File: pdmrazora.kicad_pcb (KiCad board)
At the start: 2 copper layers, 15 parts, among them J1 9-6437287-8, J2 M6_VBAT_GND, M1000 Module:mega-mcu144/0.7, U1 BTS50010-1TAD, U11 BTS7004-1EPP, U12 BTS7004-1EPP, U13 BTS7004-1EPP, U14 BTS7004-1EPP, U15 BTS7004-1EPP, U16 BTS7004-1EPP, U17 BTS7004-1EPP, U18 BTS7004-1EPP, U2 BTS50010-1TAD, U3 BTS50010-1TAD, U4 BTS50010-1TAD

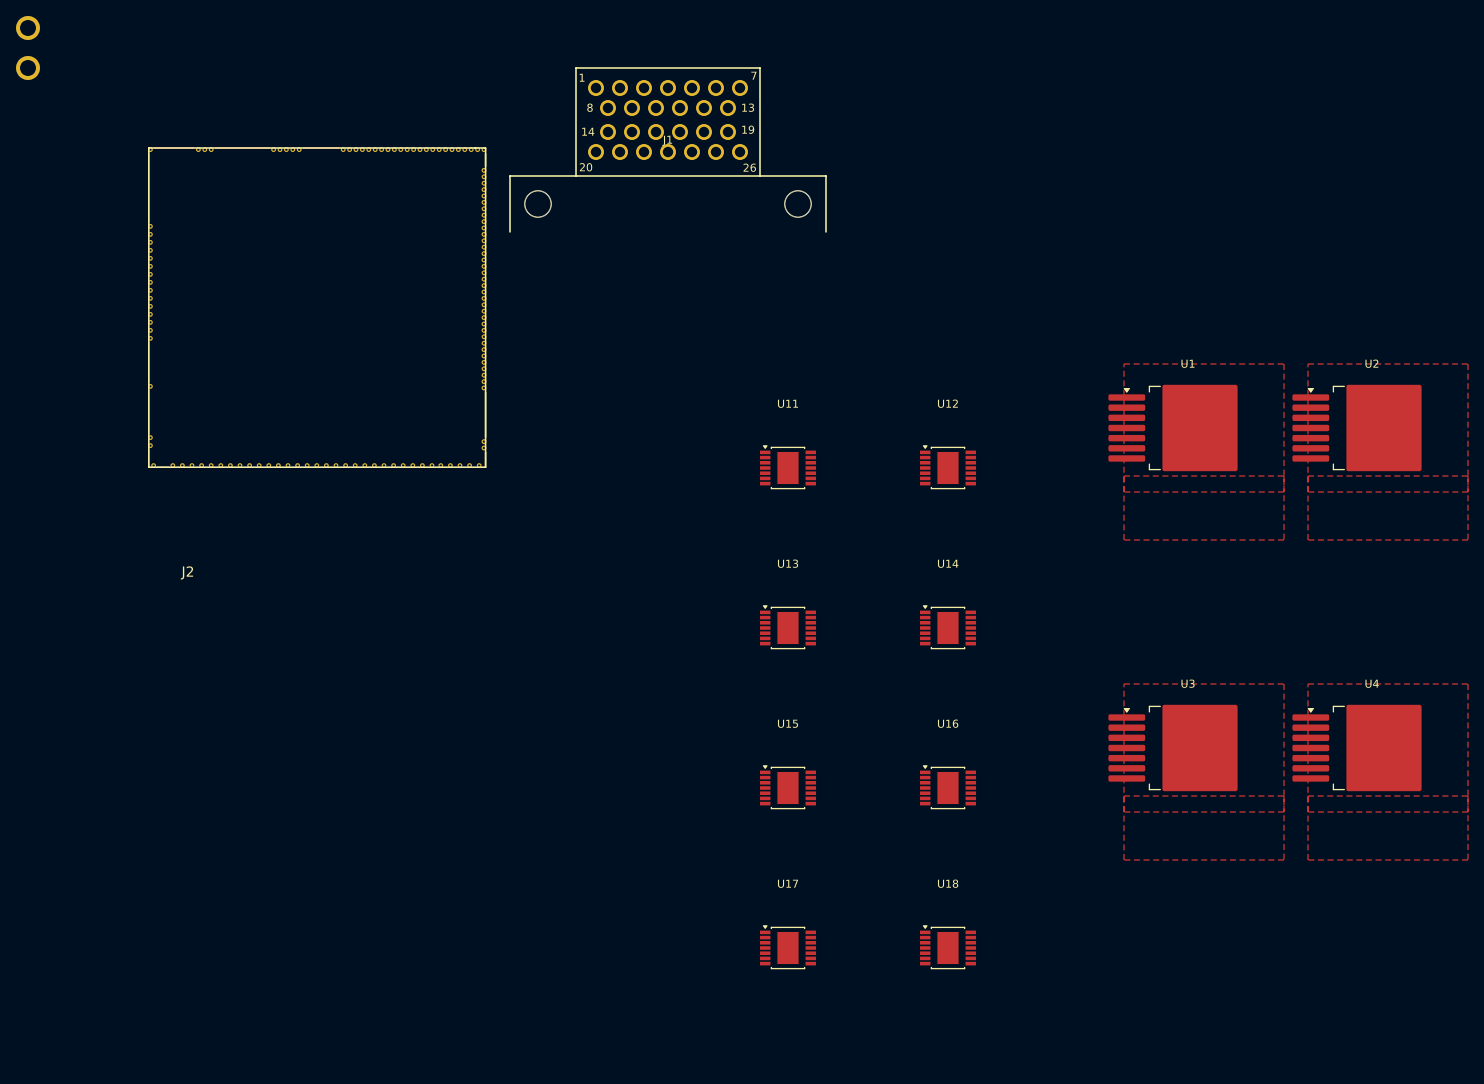
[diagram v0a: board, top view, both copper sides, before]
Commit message: Nest PDM floorplan and add power/ADIO pour scaffolding
Rearrange all 53 footprints onto a 150×130 mm Edge.Cuts board (aux
origin bottom-left), with M1000 clear for Hellen merge, J1 on the
bottom edge, HP/ADIO clustered with local sense passives, and pour
outlines for VBAT/GND/PWR_OUT/ADIO. Length routing of control/sense
remains ratsnest after fill — aggressive autoroute introduced shorts.
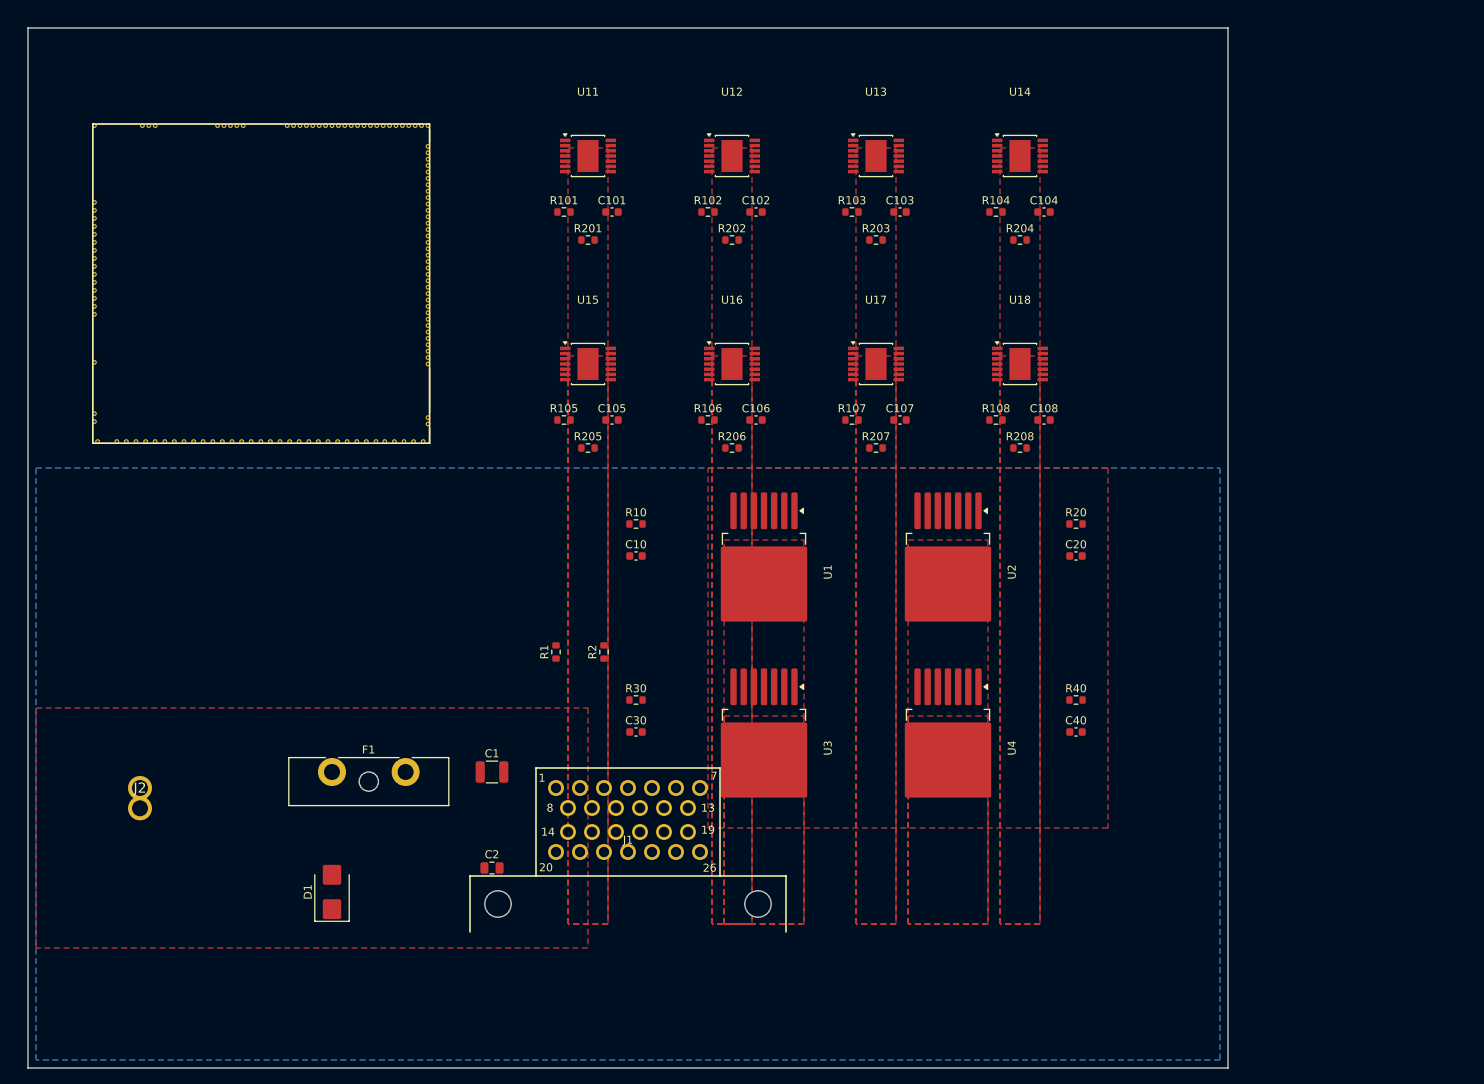
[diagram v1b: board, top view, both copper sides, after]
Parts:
- added C1: 100u_50V, C_1210_3225Metric, F.Cu at (58.0, 93.0)
- added C10: 10n, C_0603_1608Metric, F.Cu at (76.0, 66.0)
- added C101: 10n, C_0603_1608Metric, F.Cu at (73.0, 23.0)
- added C102: 10n, C_0603_1608Metric, F.Cu at (91.0, 23.0)
- added C103: 10n, C_0603_1608Metric, F.Cu at (109.0, 23.0)
- added C104: 10n, C_0603_1608Metric, F.Cu at (127.0, 23.0)
- added C105: 10n, C_0603_1608Metric, F.Cu at (73.0, 49.0)
- added C106: 10n, C_0603_1608Metric, F.Cu at (91.0, 49.0)
- added C107: 10n, C_0603_1608Metric, F.Cu at (109.0, 49.0)
- added C108: 10n, C_0603_1608Metric, F.Cu at (127.0, 49.0)
- added C2: 100n, C_0805_2012Metric, F.Cu at (58.0, 105.0)
- added C20: 10n, C_0603_1608Metric, F.Cu at (131.0, 66.0)
- added C30: 10n, C_0603_1608Metric, F.Cu at (76.0, 88.0)
- added C40: 10n, C_0603_1608Metric, F.Cu at (131.0, 88.0)
- added D1: SMBJ33CA, D_SMB, F.Cu at (38.0, 108.0)
- added F1: 150A_MEGA_TBD, Fuseholder_Blade_ATO_Littelfuse_Pudenz_2_Pin, F.Cu at (38.0, 93.0)
- added R1: 100k, R_0603_1608Metric, F.Cu at (66.0, 78.0)
- added R10: 2k7, R_0603_1608Metric, F.Cu at (76.0, 62.0)
- added R101: 4k7, R_0603_1608Metric, F.Cu at (67.0, 23.0)
- added R102: 4k7, R_0603_1608Metric, F.Cu at (85.0, 23.0)
- added R103: 4k7, R_0603_1608Metric, F.Cu at (103.0, 23.0)
- added R104: 4k7, R_0603_1608Metric, F.Cu at (121.0, 23.0)
- added R105: 4k7, R_0603_1608Metric, F.Cu at (67.0, 49.0)
- added R106: 4k7, R_0603_1608Metric, F.Cu at (85.0, 49.0)
- added R107: 4k7, R_0603_1608Metric, F.Cu at (103.0, 49.0)
- added R108: 4k7, R_0603_1608Metric, F.Cu at (121.0, 49.0)
- added R2: 10k, R_0603_1608Metric, F.Cu at (72.0, 78.0)
- added R20: 2k7, R_0603_1608Metric, F.Cu at (131.0, 62.0)
- added R201: 4k7, R_0603_1608Metric, F.Cu at (70.0, 26.5)
- added R202: 4k7, R_0603_1608Metric, F.Cu at (88.0, 26.5)
- added R203: 4k7, R_0603_1608Metric, F.Cu at (106.0, 26.5)
- added R204: 4k7, R_0603_1608Metric, F.Cu at (124.0, 26.5)
- added R205: 4k7, R_0603_1608Metric, F.Cu at (70.0, 52.5)
- added R206: 4k7, R_0603_1608Metric, F.Cu at (88.0, 52.5)
- added R207: 4k7, R_0603_1608Metric, F.Cu at (106.0, 52.5)
- added R208: 4k7, R_0603_1608Metric, F.Cu at (124.0, 52.5)
- added R30: 2k7, R_0603_1608Metric, F.Cu at (76.0, 84.0)
- added R40: 2k7, R_0603_1608Metric, F.Cu at (131.0, 84.0)
- moved J1 87.6 mm to (75.0, 109.5)
- moved U17 73.8 mm to (106.0, 42.0)
- moved U18 73.6 mm to (124.0, 42.0)
- moved U13 60.0 mm to (106.0, 16.0)
- moved U14 59.7 mm to (124.0, 16.0)
- moved U16 59.5 mm to (88.0, 42.0)
- moved U15 58.6 mm to (70.0, 42.0)
- moved U1 56.0 mm to (92.0, 68.0), turned to -90 degrees
- moved U2 56.0 mm to (115.0, 68.0), turned to -90 degrees
- moved U3 53.0 mm to (92.0, 90.0), turned to -90 degrees
- moved U4 53.0 mm to (115.0, 90.0), turned to -90 degrees
- moved U12 47.4 mm to (88.0, 16.0)
- moved U11 46.3 mm to (70.0, 16.0)
- moved J2 27.7 mm to (14.0, 95.0)
- moved M1000 7.62 mm to (8.00, 52.0)
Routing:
- added copper zone on F.Cu, net ADIO1
- added copper zone on F.Cu, net ADIO2
- added copper zone on F.Cu, net ADIO3
- added copper zone on F.Cu, net ADIO4
- added copper zone on F.Cu, net ADIO5
- added copper zone on F.Cu, net ADIO6
- added copper zone on F.Cu, net ADIO7
- added copper zone on F.Cu, net ADIO8
- added copper zone on B.Cu, net GND
- added copper zone on F.Cu, net GND
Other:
- board outline added: 150 x 130 mm

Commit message: Fill pours and selectively route copper on pdmrazora
Complete zone fills for VBAT/GND/PWR_OUT/ADIO (M1000 keepout
respected) and add selective Manhattan tracks + vias for power
entry, HP/ADIO outs, local sense, IGN/CAN/SENSOR spines, and
EN/IS stubs to M1000. Tracks 0→328, DRC unconnected 254→97.
KiCad 8 headers preserved after pcbnew 9 save. Interactive DRC
cleanup of remaining shorts/crossings still needed.
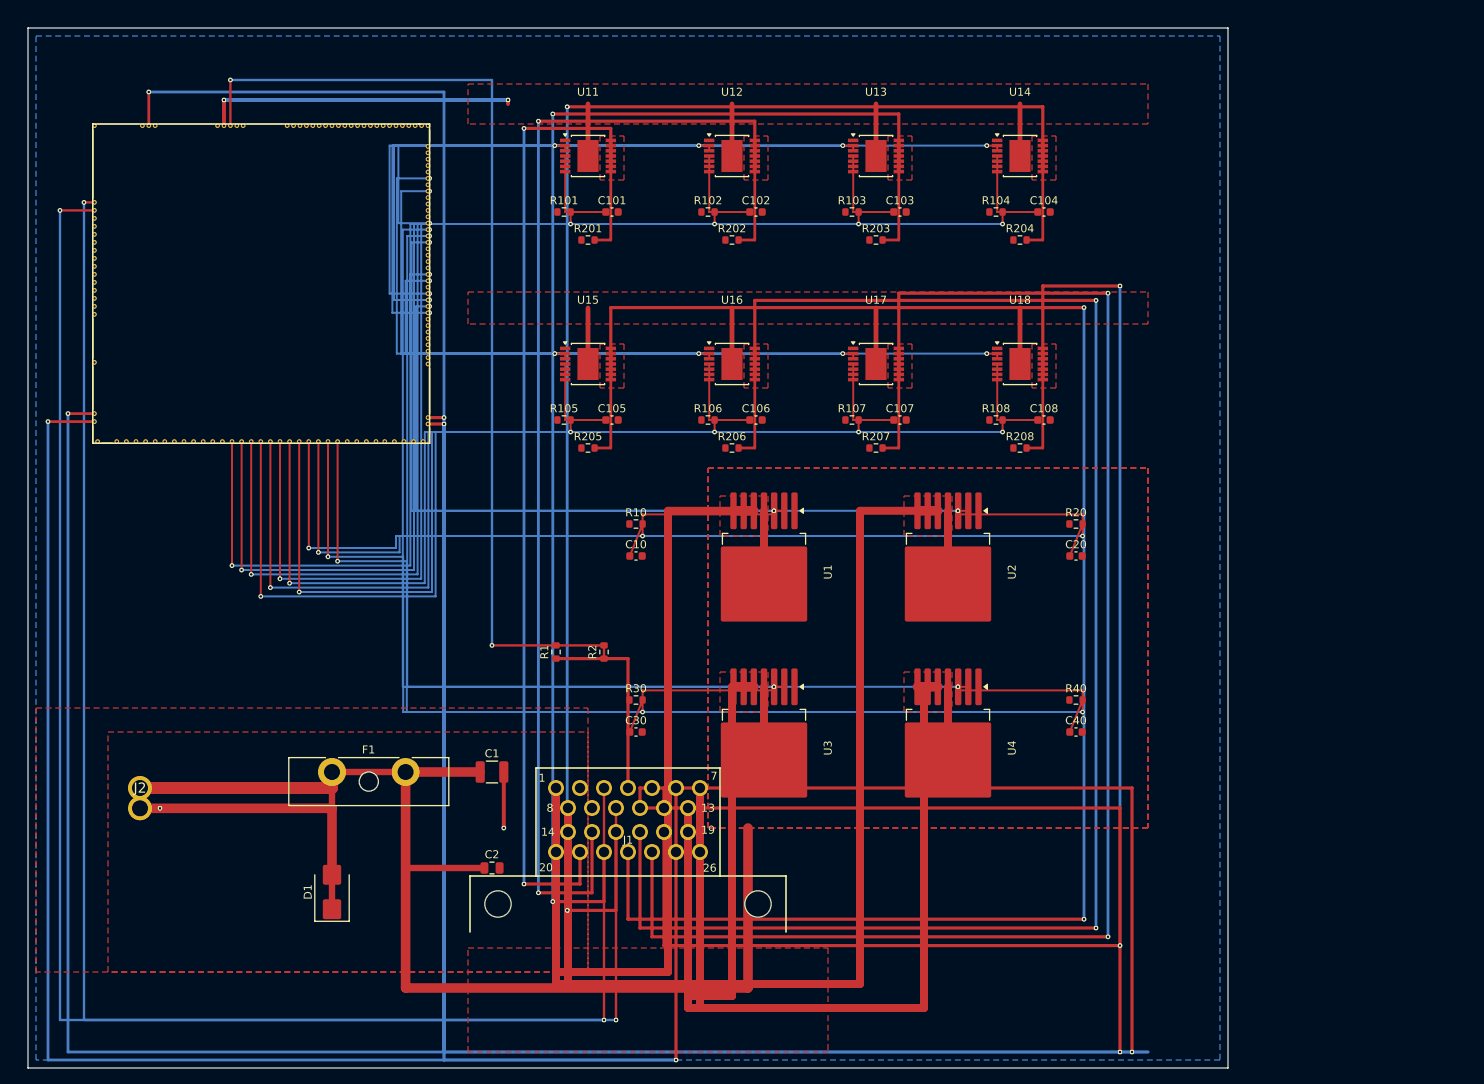
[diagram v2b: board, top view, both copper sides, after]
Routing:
- net SENSOR_5V: track 0.00 -> 568.7 mm, vias 0 -> 5
- net VBAT: track 0.00 -> 303.1 mm, vias 0 -> 2
- net SENSOR_GND: track 0.00 -> 283.6 mm, vias 0 -> 3
- net ADIO5: track 0.00 -> 220.6 mm, vias 0 -> 2
- net ADIO6: track 0.00 -> 210.6 mm, vias 0 -> 2
- net CANH: track 0.00 -> 202.5 mm, vias 0 -> 2
- net CANL: track 0.00 -> 196.5 mm, vias 0 -> 2
- net ADIO7: track 0.00 -> 195.6 mm, vias 0 -> 2
- net ADIO4: track 0.00 -> 194.5 mm, vias 0 -> 2
- net PWR_OUT2: track 0.00 -> 191.2 mm
- net ADIO8: track 0.00 -> 185.6 mm, vias 0 -> 2
- net ADIO3: track 0.00 -> 172.1 mm, vias 0 -> 2
- net IN_O2S: track 0.00 -> 165.4 mm, vias 0 -> 2
- net ADIO2: track 0.00 -> 154.7 mm, vias 0 -> 2
- net IN_AUX4: track 0.00 -> 149.9 mm, vias 0 -> 2
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
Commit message: Clear DRC shorts/crossings; SENSOR_5V PU taps and GND stitches
Surgical UUID-based conflict deletes plus gated PWR/ADIO/CAN restore
bring shorts 94→1 (J2 header only) and crossings 110→33. SENSOR_5V
taps to R201–R208 and GND stitch vias added. KiCad 8 format kept;
HELLCORE untouched. Unconnected rises (conflict copper removed).
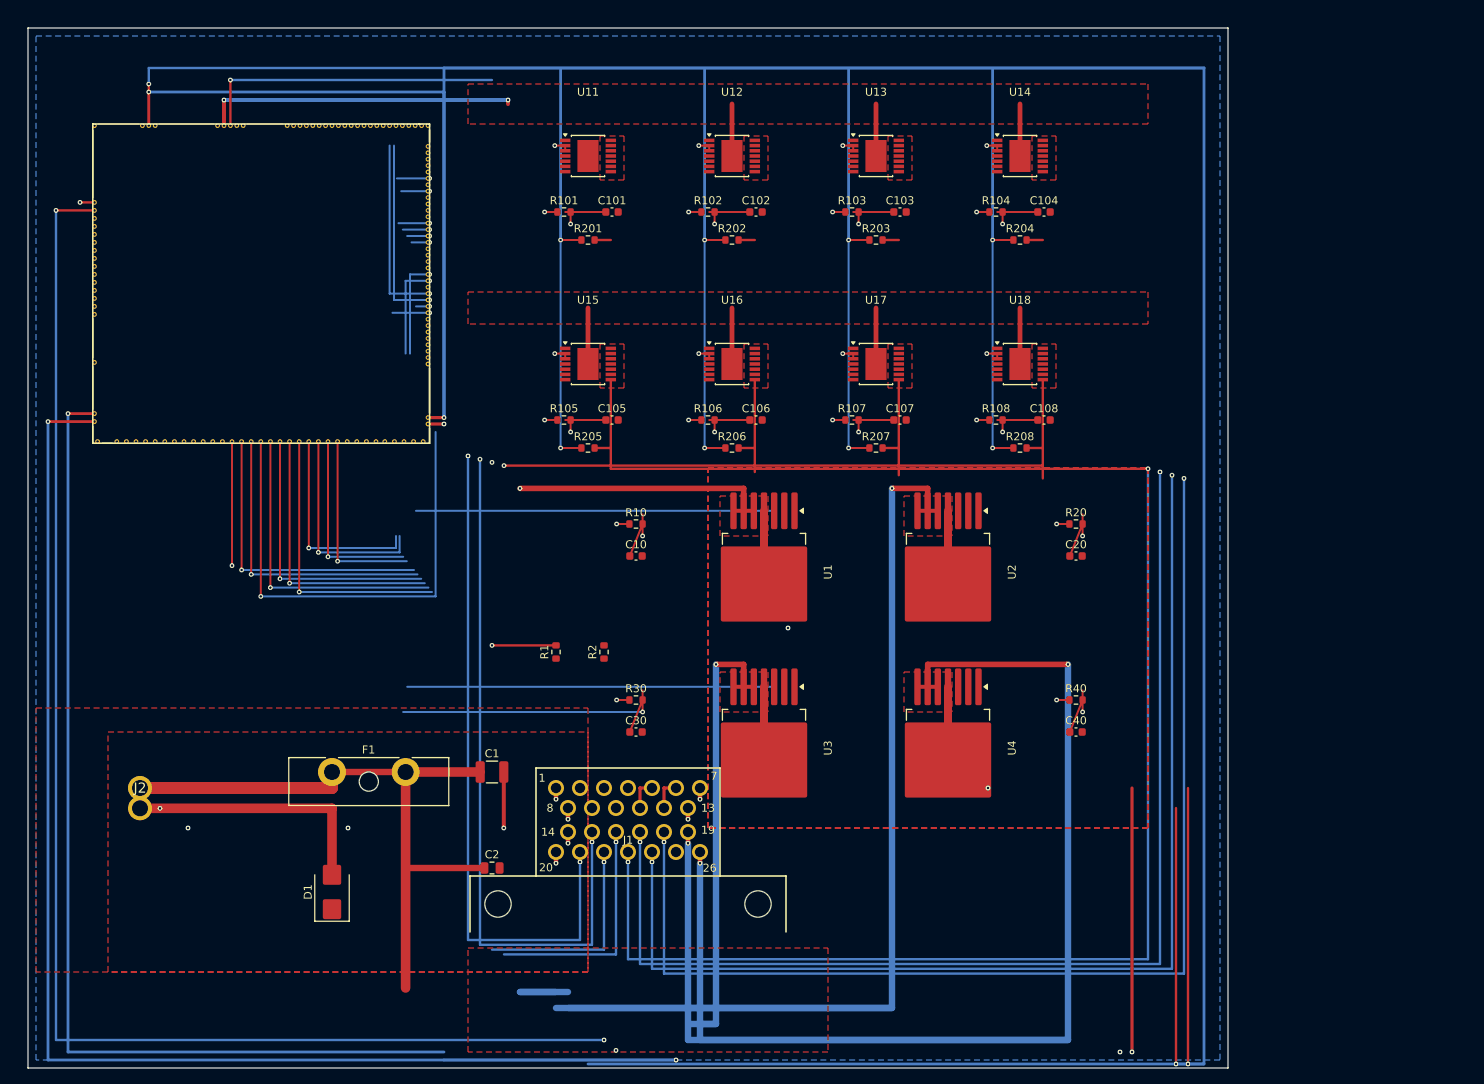
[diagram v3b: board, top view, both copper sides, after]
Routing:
- net SENSOR_5V: track 568.7 -> 1004.0 mm, vias 5 -> 16
- net CANL: track 196.5 -> 1.80 mm
- net ADIO3: track 172.1 -> 28.2 mm
- net OUT_PWM4: track 131.4 -> 3.55 mm, vias 2 -> 1
- net IN_O2S: track 165.4 -> 41.4 mm
- net IN_AUX4: track 149.9 -> 31.1 mm
- net SENSOR_GND: track 283.6 -> 170.1 mm
- net IN_MAP3: track 149.9 -> 44.0 mm
- net OUT_PWM2: track 105.6 -> 2.45 mm, vias 2 -> 1
- net IN_AUX2: track 134.4 -> 33.1 mm
- net ADIO4: track 194.5 -> 98.7 mm
- net OUT_PWM8: track 102.0 -> 6.80 mm
- net IN_MAP1: track 114.1 -> 22.1 mm
- net IN_MAP2: track 132.0 -> 44.2 mm
- net VBAT: track 303.1 -> 216.7 mm, vias 2 -> 3
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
